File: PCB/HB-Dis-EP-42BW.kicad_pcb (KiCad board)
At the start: 2 copper layers, 61.4 x 103.3 mm, 42 parts, among them J1 Reset, J2 FTDI, J3 ISP, J4 ePaper, J5 ePaper_TestPoints, J6 Supply, J7 Conn_GPIO, J8 Config, J9 Conn_I2C, Q1 IRLML6344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

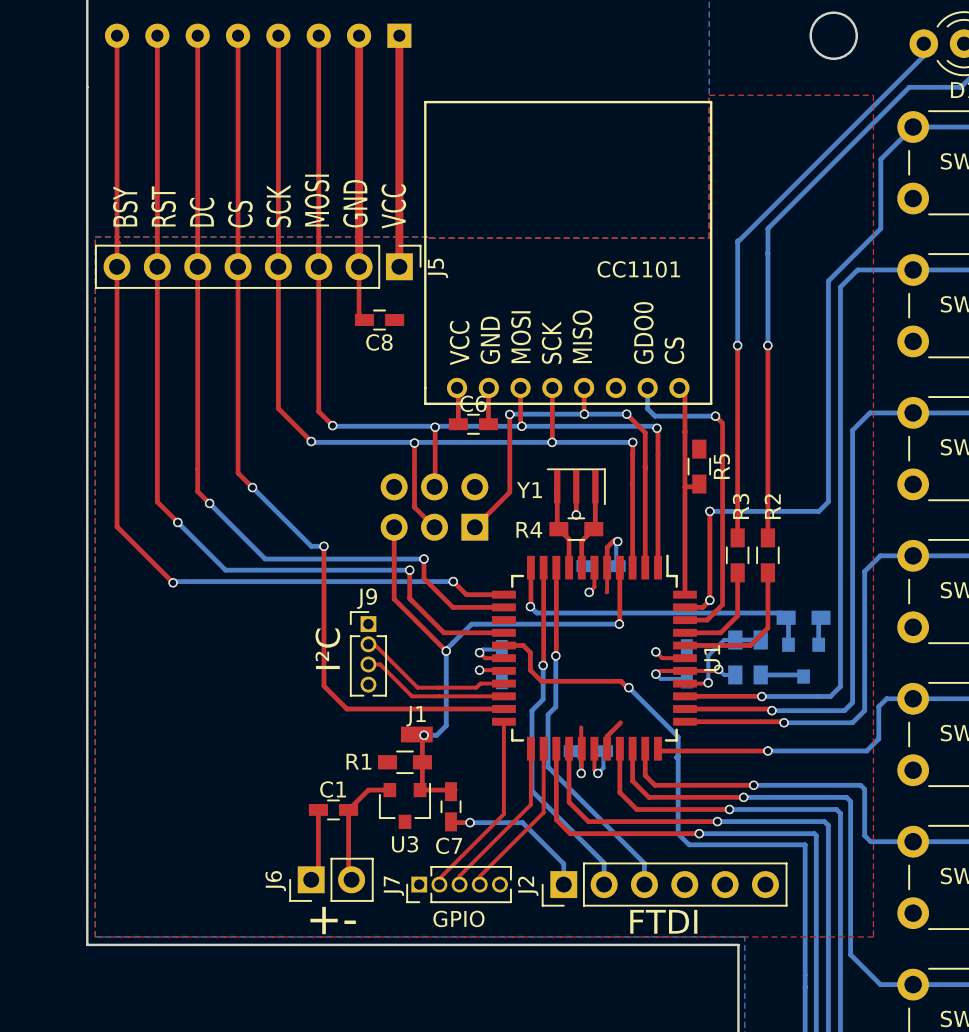
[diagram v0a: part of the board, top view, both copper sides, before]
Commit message: replace VCC layer by net
as suggested by TomMajor
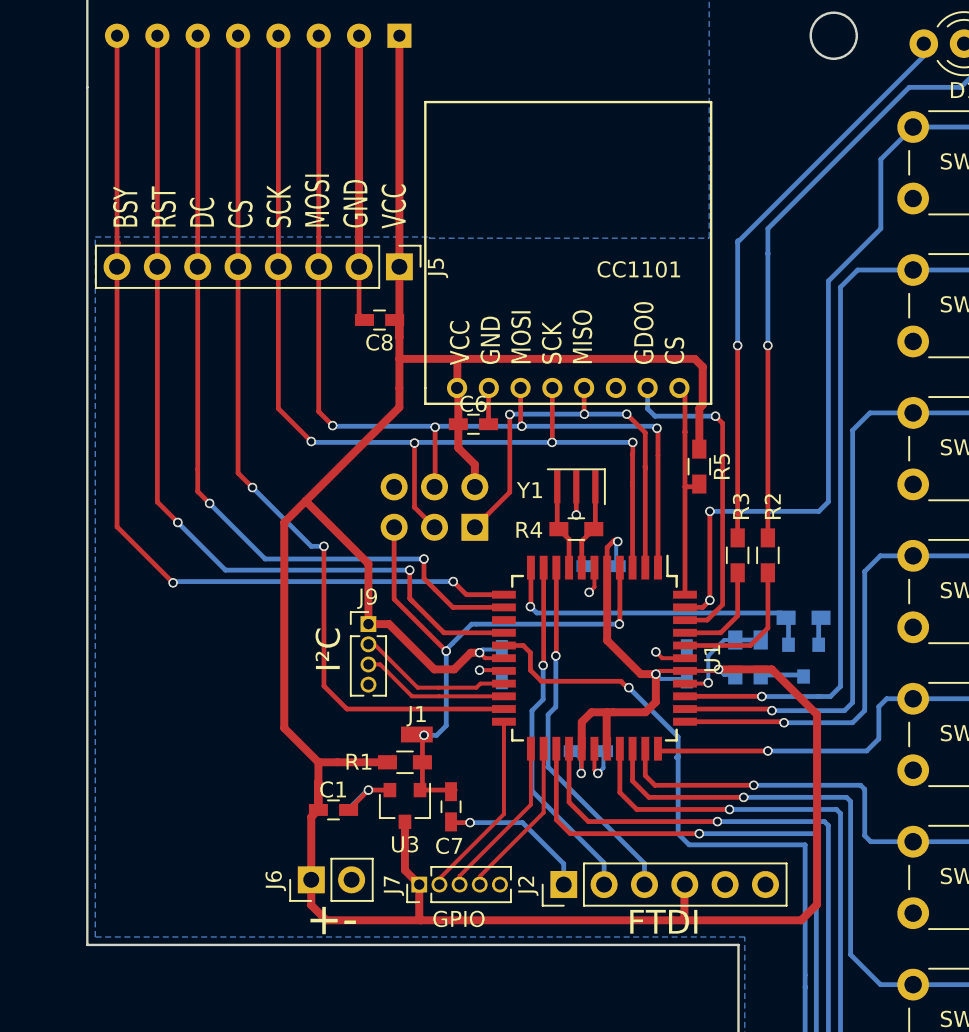
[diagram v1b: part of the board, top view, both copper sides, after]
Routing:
- net VCC: track 45.2 -> 219.6 mm
- net GND: track 40.4 -> 38.0 mm, vias 5 -> 6
- removed copper zone on F.Cu, net VCC

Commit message: small PCB improvments
- enlarge VCC where connected to pads
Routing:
- net VCC: track 219.6 -> 218.4 mm

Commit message: last PCB improvements for V1.0
- put correct mounting holes
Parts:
- added REF**: MountingHole_4mm, Mounting_Holes:MountingHole_4mm, F.Cu at (114.3, 133.3)
- added REF**: MountingHole_3.2mm_M3, Mounting_Holes:MountingHole_3.2mm_M3, F.Cu at (106.0, 36.8)
- added REF**: MountingHole_3.2mm_M3, Mounting_Holes:MountingHole_3.2mm_M3, F.Cu at (106.0, 133.8)
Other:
- outline, holes or cut-outs redrawn
- board text added: "HB-Dis-EP-42BW"
- board text added: "stan23 V1.0 Feb 2019 CC BY-NC-SA 3.0"
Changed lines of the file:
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@@
     (area 14.550001 23.80008 137.564366 146.10008)
     (thickness 1.6)
-    (drawings 27)
+    (drawings 26)
     (tracks 515)
     (zones 0)
-    (modules 42)
+    (modules 45)
     (nets 43)
   )
@@
     (40 Dwgs.User user)
     (41 Cmts.User user)
-    (42 Eco1.User user)
-    (43 Eco2.User user)
+    (42 Eco1.User user hide)
+    (43 Eco2.User user hide)
     (44 Edge.Cuts user)
     (45 Margin user hide)
@@
   )
   (setup
-    (last_trace_width 0.5)
+    (last_trace_width 0.25)
     (user_trace_width 0.3)
     (user_trace_width 0.5)
@@
     (add_net VCC)
   )
+  (module Mounting_Holes:MountingHole_4mm (layer F.Cu)
+    (at 114.25008 133.25008)
+    (descr "Mounting Hole 4mm, no annular")
+    (tags "mounting hole 4mm no annular")
+    (attr virtual)
+    (fp_text reference REF** (at -0.2 4.65) (layer F.SilkS)
+      (effects (font (size 1 1) (thickness 0.15)))
+    )
+    (fp_text value MountingHole_4mm (at 0 5) (layer F.Fab)
+      (effects (font (size 1 1) (thickness 0.15)))
+    )
+    (fp_text user %R (at 0.3 0) (layer F.Fab)
+      (effects (font (size 1 1) (thickness 0.15)))
+    )
+    (fp_circle (center 0 0) (end 4 0) (layer Cmts.User) (width 0.15))
+    (fp_circle (center 0 0) (end 4.25 0) (layer F.CrtYd) (width 0.05))
+    (pad 1 np_thru_hole circle (at 0 0) (size 4 4) (drill 4) (layers *.Cu *.Mask))
+  )
   (module Capacitors_SMD:C_0603_HandSoldering (layer F.Cu)
     (at 74.50008 85.50008)
@@
     )
   )
+  (module Mounting_Holes:MountingHole_3.2mm_M3 (layer F.Cu)
+    (at 106.00008 36.75008)
+    (descr "Mounting Hole 3.2mm, no annular, M3")
+    (tags "mounting hole 3.2mm no annular m3")
+    (attr virtual)
+    (fp_text reference REF** (at 0 -4.2) (layer F.SilkS)
+      (effects (font (size 1 1) (thickness 0.15)))
+    )
+    (fp_text value MountingHole_3.2mm_M3 (at 0 4.2) (layer F.Fab)
+      (effects (font (size 1 1) (thickness 0.15)))
+    )
+    (fp_text user %R (at 0.3 0) (layer F.Fab)
+      (effects (font (size 1 1) (thickness 0.15)))
+    )
+    (fp_circle (center 0 0) (end 3.2 0) (layer Cmts.User) (width 0.15))
+    (fp_circle (center 0 0) (end 3.45 0) (layer F.CrtYd) (width 0.05))
+    (pad 1 np_thru_hole circle (at 0 0) (size 3.2 3.2) (drill 3.2) (layers *.Cu *.Mask))
+  )
+  (module Mounting_Holes:MountingHole_3.2mm_M3 (layer F.Cu)
+    (at 106.00008 133.75008)
+    (descr "Mounting Hole 3.2mm, no annular, M3")
+    (tags "mounting hole 3.2mm no annular m3")
+    (attr virtual)
+    (fp_text reference REF** (at 0.05 4.2) (layer F.SilkS)
+      (effects (font (size 1 1) (thickness 0.15)))
+    )
+    (fp_text value MountingHole_3.2mm_M3 (at 0 4.2) (layer F.Fab)
+      (effects (font (size 1 1) (thickness 0.15)))
+    )
+    (fp_text user %R (at 0.3 0) (layer F.Fab)
+      (effects (font (size 1 1) (thickness 0.15)))
+    )
+    (fp_circle (center 0 0) (end 3.2 0) (layer Cmts.User) (width 0.15))
+    (fp_circle (center 0 0) (end 3.45 0) (layer F.CrtYd) (width 0.05))
+    (pad 1 np_thru_hole circle (at 0 0) (size 3.2 3.2) (drill 3.2) (layers *.Cu *.Mask))
+  )
+  (gr_text HB-Dis-EP-42BW (at 83.50008 39.65008) (layer B.SilkS)
+    (effects (font (size 2 2) (thickness 0.5)) (justify mirror))
+  )
+  (gr_text "stan23\nV1.0  Feb 2019\nCC BY-NC-SA 3.0" (at 97.25008 45.35008) (layer B.SilkS)
+    (effects (font (size 1.5 1.5) (thickness 0.3)) (justify left mirror))
+  )
   (gr_line (start 120.40008 137.10008) (end 120.40008 33.80008) (angle 90) (layer Edge.Cuts) (width 0.15))
   (gr_text Config (at 101.40008 124.50008 90) (layer F.SilkS)
@@
     (effects (font (size 1.5 1.5) (thickness 0.3)) (justify mirror))
   )
-  (gr_circle (center 114.25008 133.25008) (end 114.25008 135.25008) (layer Edge.Cuts) (width 0.15))
   (gr_line (start 100.00008 137.10008) (end 100.00008 94.00008) (angle 90) (layer Edge.Cuts) (width 0.15))
   (gr_line (start 100.00008 137.10008) (end 120.40008 137.10008) (angle 90) (layer Edge.Cuts) (width 0.15))
@@
     (arrow2b (pts (xy 129.00008 136.40008) (xy 128.413659 135.273576)))
   )
-  (gr_circle (center 106 36.75) (end 107.05 37.75) (layer Edge.Cuts) (width 0.15))
-  (gr_circle (center 106 133.75) (end 107.4 134.35) (layer Edge.Cuts) (width 0.15))
   (gr_line (start 59.00008 33.80008) (end 120.40008 33.80008) (angle 90) (layer Edge.Cuts) (width 0.15))
   (gr_line (start 59.00008 40.00008) (end 59.00008 33.80008) (angle 90) (layer Edge.Cuts) (width 0.15))
@@
     (arrow2b (pts (xy 31.5 137.799999) (xy 32.626504 137.213578)))
   )
-  (segment (start 90.13208 81.64608) (end 90.13208 83.16808) (width 0.5) (layer F.Cu) (net 1) (status 400000))
+  (segment (start 90.13208 81.64608) (end 90.13208 83.16808) (width 0.5) (layer F.Cu) (net 1))
   (segment (start 90.13208 83.16808) (end 90.10008 83.20008) (width 0.5) (layer F.Cu) (net 1))
-  (segment (start 91.73208 70.24608) (end 91.73208 69.26808) (width 0.5) (layer F.Cu) (net 1) (status 400000))
+  (segment (start 91.73208 70.24608) (end 91.73208 69.26808) (width 0.5) (layer F.Cu) (net 1))
   (segment (start 92.30008 68.70008) (end 92.40008 68.60008) (width 0.25) (layer B.Cu) (net 1))
   (via (at 92.40008 68.60008) (size 0.6) (drill 0.4) (layers F.Cu B.Cu) (net 1))
   (segment (start 92.30008 68.70008) (end 92.30008 70.15008) (width 0.25) (layer B.Cu) (net 1))
   (segment (start 91.73208 69.26808) (end 92.40008 68.60008) (width 0.5) (layer F.Cu) (net 1))
-  (segment (start 96.63208 76.74608) (end 95.00408 76.74608) (width 0.5) (layer F.Cu) (net 1) (status 400000))
+  (segment (start 96.63208 76.74608) (end 95.00408 76.74608) (width 0.5) (layer F.Cu) (net 1))
   (segment (start 95.00408 76.74608) (end 94.80008 76.95008) (width 0.5) (layer F.Cu) (net 1))
-  (segment (start 96.63208 76.74608) (end 98.65408 76.74608) (width 0.5) (layer F.Cu) (net 1) (status 400000))
+  (segment (start 96.63208 76.74608) (end 98.65408 76.74608) (width 0.5) (layer F.Cu) (net 1))
   (segment (start 98.65408 76.74608) (end 98.75008 76.65008) (width 0.5) (layer F.Cu) (net 1))
-  (segment (start 91.73208 81.64608) (end 91.73208 79.38208) (width 0.5) (layer F.Cu) (net 1) (status 400000))
+  (segment (start 91.73208 81.64608) (end 91.73208 79.38208) (width 0.5) (layer F.Cu) (net 1))
   (segment (start 91.73208 79.38208) (end 91.70008 79.35008) (width 0.5) (layer F.Cu) (net 1))
-  (segment (start 85.23208 75.94608) (end 84.04608 75.94608) (width 0.5) (layer F.Cu) (net 1) (status 400000))
+  (segment (start 85.23208 75.94608) (end 84.04608 75.94608) (width 0.5) (layer F.Cu) (net 1))
   (segment (start 84.04608 75.94608) (end 83.70008 75.60008) (width 0.5) (layer F.Cu) (net 1))
   (segment (start 96.60008 92.45008) (end 96.60008 90.22008) (width 0.5) (layer F.Cu) (net 1))
@@
   (segment (start 91.73208 81.64608) (end 91.69408 81.68408) (width 0.3) (layer F.Cu) (net 1))
   (segment (start 81.95 59.05) (end 82 59) (width 0.3) (layer F.Cu) (net 1))
-  (segment (start 90.93208 81.64608) (end 90.93208 82.98208) (width 0.5) (layer F.Cu) (net 2) (status 400000))
+  (segment (start 90.93208 81.64608) (end 90.93208 82.98208) (width 0.5) (layer F.Cu) (net 2))
   (via (at 91.15008 83.20008) (size 0.6) (drill 0.4) (layers F.Cu B.Cu) (net 2))
   (segment (start 91.15008 83.20008) (end 91.50008 82.85008) (width 0.25) (layer B.Cu) (net 2))
   (segment (start 91.50008 82.85008) (end 91.50008 81.80008) (width 0.25) (layer B.Cu) (net 2))
   (segment (start 90.93208 82.98208) (end 91.15008 83.20008) (width 0.5) (layer F.Cu) (net 2))
-  (segment (start 90.93208 70.24608) (end 90.93208 71.46808) (width 0.5) (layer F.Cu) (net 2) (status 400000))
+  (segment (start 90.93208 70.24608) (end 90.93208 71.46808) (width 0.5) (layer F.Cu) (net 2))
   (via (at 90.60008 71.80008) (size 0.6) (drill 0.4) (layers F.Cu B.Cu) (net 2))
   (segment (start 90.93208 71.46808) (end 90.60008 71.80008) (width 0.5) (layer F.Cu) (net 2))
-  (segment (start 96.63208 75.94608) (end 95.19608 75.94608) (width 0.5) (layer F.Cu) (net 2) (status 400000))
+  (segment (start 96.63208 75.94608) (end 95.19608 75.94608) (width 0.5) (layer F.Cu) (net 2))
   (via (at 94.80008 75.55008) (size 0.6) (drill 0.4) (layers F.Cu B.Cu) (net 2))
   (segment (start 95.19608 75.94608) (end 94.80008 75.55008) (width 0.5) (layer F.Cu) (net 2))
-  (segment (start 85.23208 76.74608) (end 83.74608 76.74608) (width 0.5) (layer F.Cu) (net 2) (status 400000))
+  (segment (start 85.23208 76.74608) (end 83.74608 76.74608) (width 0.5) (layer F.Cu) (net 2))
   (via (at 83.70008 76.70008) (size 0.6) (drill 0.4) (layers F.Cu B.Cu) (net 2))
   (segment (start 83.74608 76.74608) (end 83.70008 76.70008) (width 0.5) (layer F.Cu) (net 2))

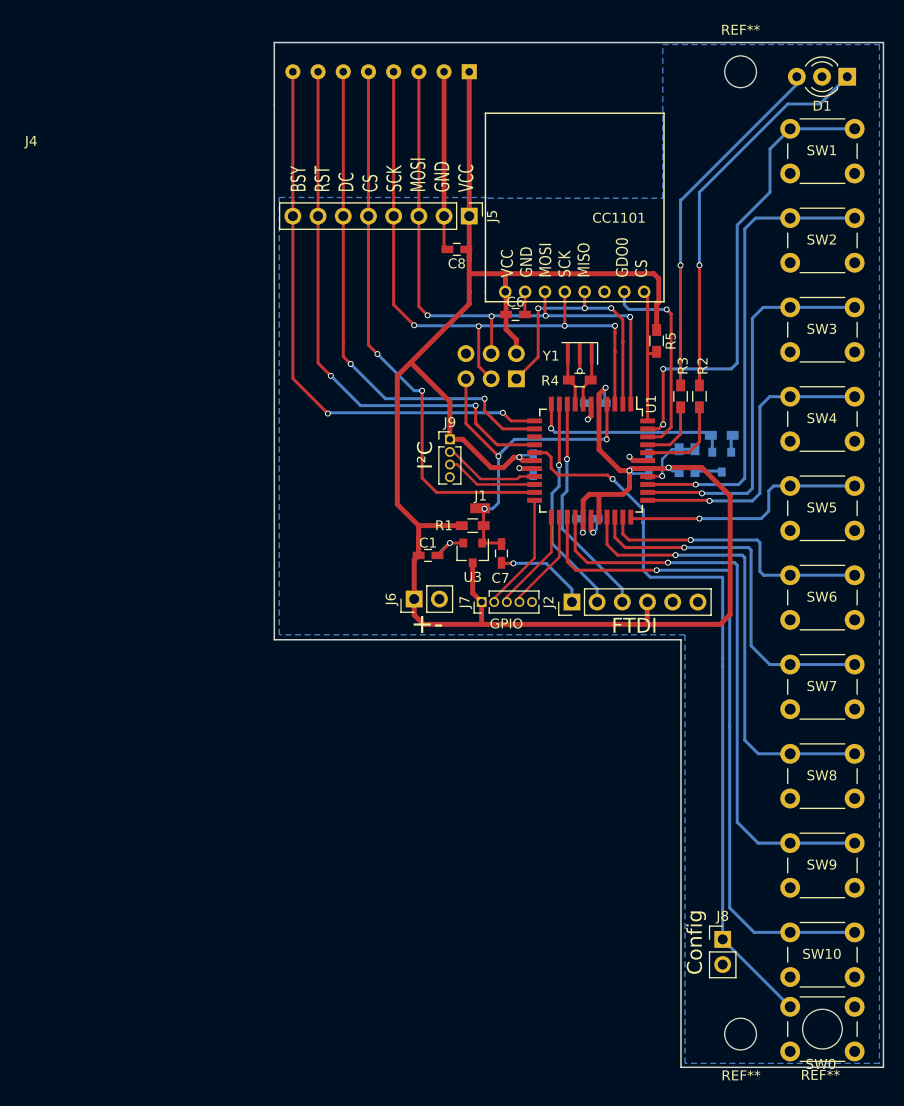
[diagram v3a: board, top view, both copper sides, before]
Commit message: PCB V1.1
- fix spacing and placement of buttons (8.5 mm instead of 9.0 mm)
- add hole for CC1101 antenna
- move battery connector a bit
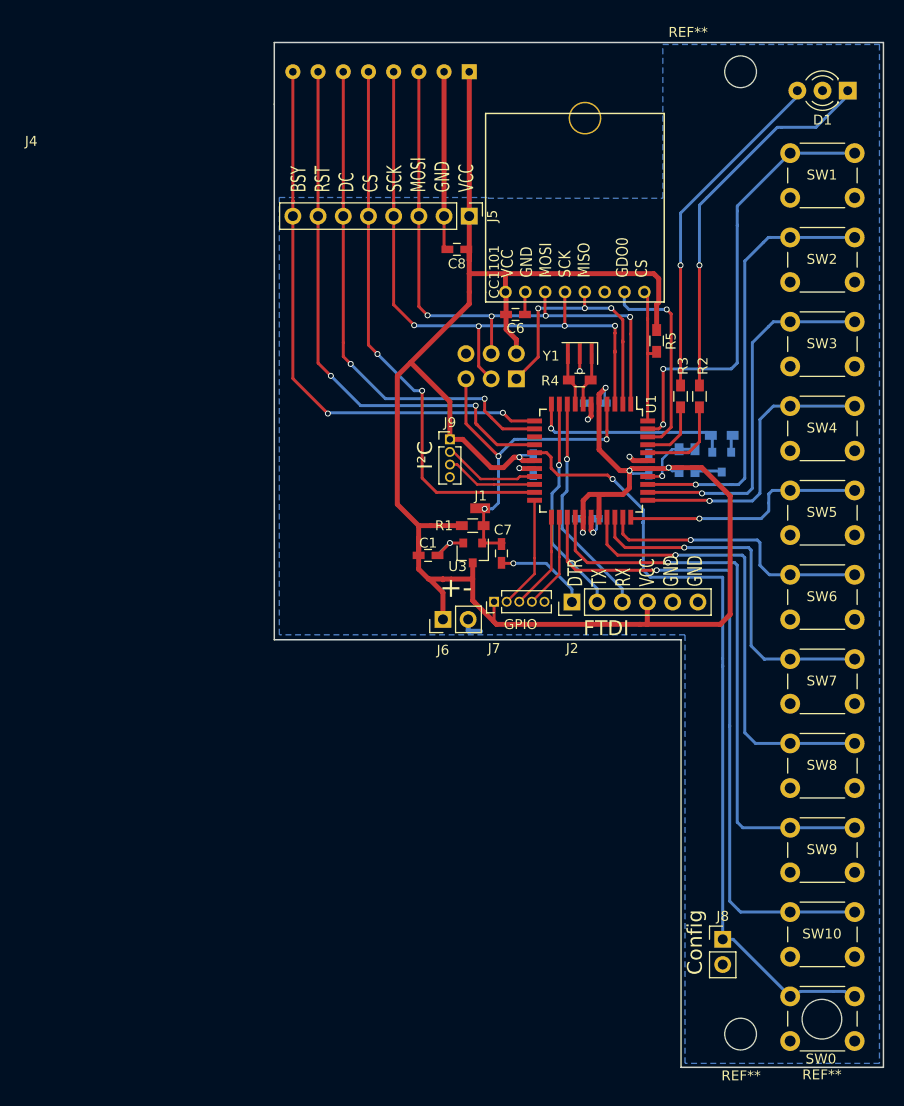
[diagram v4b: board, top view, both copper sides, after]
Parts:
- R2, R3: value R -> 300
- R7: value 8.2 -> 30
- R8: value 8.2 -> 10
- moved J6 3.55 mm to (76.0, 92.0)
- moved SW1 2.45 mm to (111.0, 45.0)
- moved SW10 2.05 mm to (111.0, 121.5)
- moved SW2 1.95 mm to (111.0, 53.5)
- moved SW9 1.55 mm to (111.0, 113.0)
- moved SW3 1.45 mm to (111.0, 62.0)
- moved D1 1.40 mm to (116.8, 38.7)
- moved J7 1.25 mm to (81.2, 90.2)
- moved SW8 1.05 mm to (111.0, 104.5)
- moved SW0 1.05 mm to (111.0, 130.0)
- moved REF** 1.00 mm to (114.2, 132.3)
- moved SW4 0.95 mm to (111.0, 70.5)
- moved SW7 0.55 mm to (111.0, 96.0)
- moved SW5 0.45 mm to (111.0, 79.0)
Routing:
- net /CONFIG: track 74.7 -> 82.2 mm
- net /BTN2: track 46.9 -> 44.2 mm
- net /BTN1: track 47.4 -> 45.0 mm
- net GND: track 38.1 -> 40.3 mm
- net /BTN3: track 38.7 -> 36.7 mm
- net Net-(D1-Pad3): track 36.1 -> 34.1 mm
- net Net-(D1-Pad1): track 39.3 -> 37.7 mm
- net /BTN10: track 68.9 -> 67.7 mm
- net /BTN4: track 30.4 -> 29.2 mm
- net VCC: track 218.4 -> 217.4 mm
- net /BTN8: track 47.3 -> 46.4 mm
- net /BTN9: track 58.9 -> 58.3 mm
- net /GPIO3: track 10.2 -> 9.67 mm
- net /GPIO1: track 11.9 -> 11.4 mm
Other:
- board text added: "DTR TX RX VCC GND GND"
- board text added: "stan23 V1.1 March 2019 CC BY-NC-SA 3.0"
- board text removed: "stan23 V1.0 Feb 2019 CC BY-NC-SA 3.0"

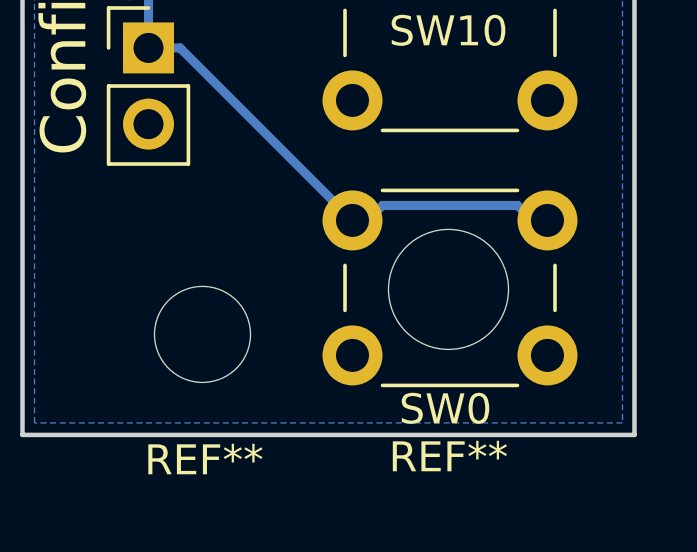
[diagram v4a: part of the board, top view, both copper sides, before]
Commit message: Update HB-Dis-EP-42BW.kicad_pcb
- move config button to bottom of pcb
- fix some 3D symbols
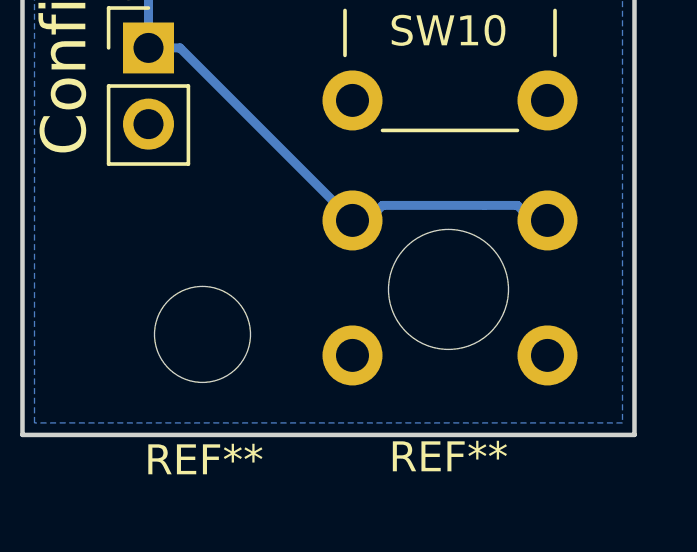
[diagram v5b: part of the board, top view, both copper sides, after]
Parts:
- SW0: moved to B.Cu
- moved SW0 6.50 mm to (117.5, 130.0), turned to 180 degrees
